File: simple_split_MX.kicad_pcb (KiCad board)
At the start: 2 copper layers, 182.1 x 114.5 mm, 120 parts, among them J1 AudioJack3, J2 Conn_01x02, M1 MountingHole, M10 MountingHole, M11 MountingHole, M2 MountingHole, M3 MountingHole, M4 MountingHole, M5 MountingHole, M6 MountingHole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

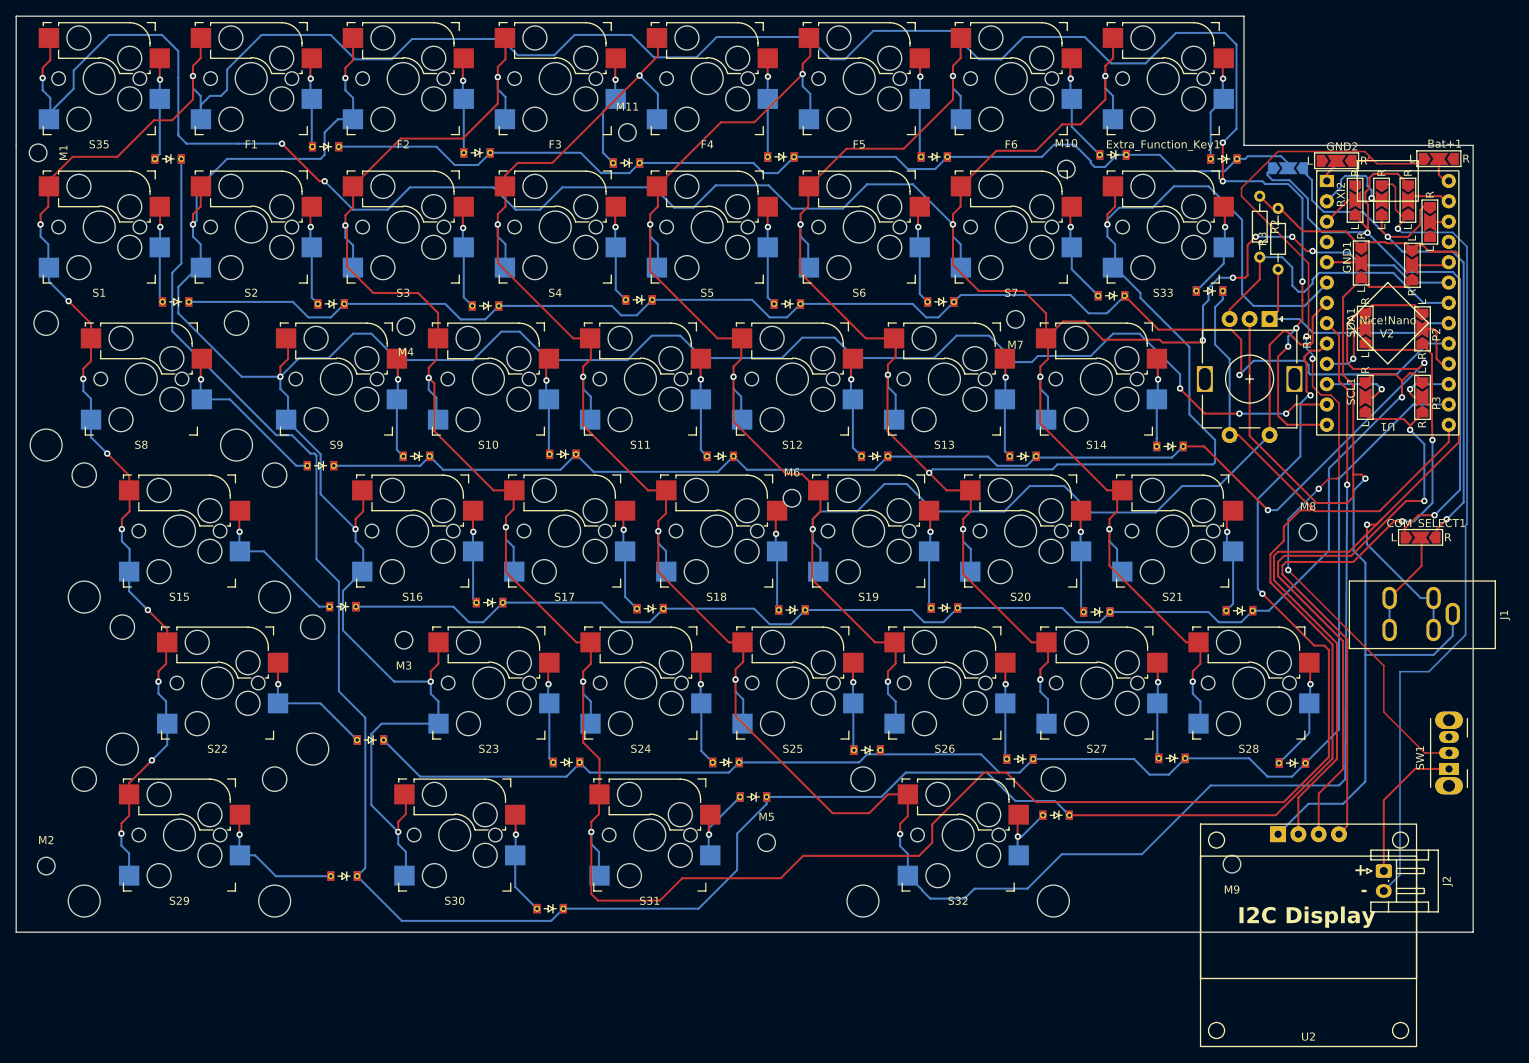
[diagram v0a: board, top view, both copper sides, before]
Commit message: updated board to remove unused vias
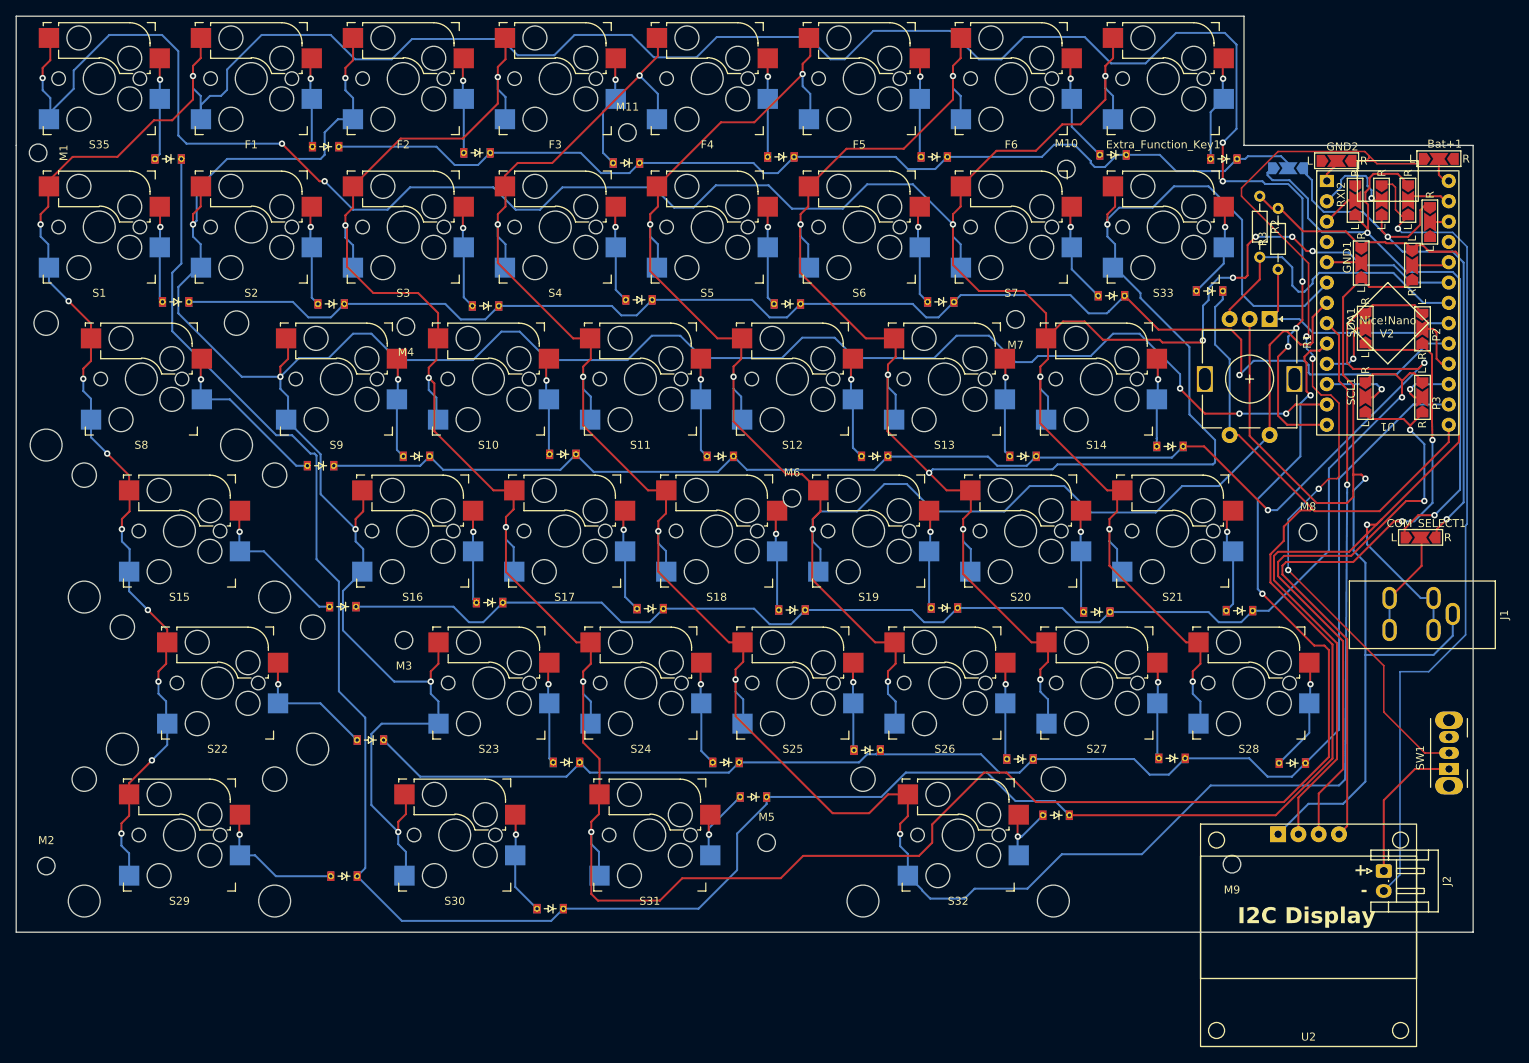
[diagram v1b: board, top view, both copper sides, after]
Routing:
- net /G: track 367.2 -> 363.2 mm
- net /C: track 344.6 -> 341.7 mm
- net /A: track 351.8 -> 349.5 mm
- net /E: track 233.6 -> 231.3 mm
- net /B: track 333.1 -> 330.9 mm
- net /F: track 263.4 -> 261.2 mm
- net /D: track 303.8 -> 301.8 mm
- net /5: track 336.9 -> 335.8 mm
- net /Bat+: track 119.6 -> 118.7 mm
- net /Bat-: track 106.0 -> 105.2 mm
- net Net-(P3-COM): track 7.97 -> 7.33 mm
- net /SCL: track 79.2 -> 78.7 mm
